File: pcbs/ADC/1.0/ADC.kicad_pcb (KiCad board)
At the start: 2 copper layers, 85 x 55 mm, 44 parts, among them J1 Conn_01x04_Pin, J3 Conn_01x02_Male, J4 Conn_01x03_Pin, J5 Conn_01x03_Pin, J9 Conn_01x04_Pin, U1 ZLDO1117QG33TA, U2 PCM1863, Y1 24.576 MHz

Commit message: Updating PCBs
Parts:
- moved C18 3.06 mm to (126.1, 102.4)
- moved R9 3.06 mm to (122.2, 102.4)
- moved C16 0.14 mm to (120.6, 92.1)
- renumbered C20 to C1, C4 to C10, C18 to C11, C19 to C12, C10 to C13, C11 to C14, C12 to C15, C13 to C16, C14 to C18, C15 to C19, C1 to C2, C16 to C20, C2 to C3, C6 to C4, C7 to C6, C8 to C7, C3 to C8, J3 to J2, J4 to J3, J9 to J4, R3 to R1, R8 to R2, R9 to R3, R1 to R4, R7 to R5, R2 to R7, R5 to R8, R4 to R9
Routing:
- net 3V3: track 120.4 -> 115.4 mm, vias 4 -> 2
- net 3V3A: track 83.7 -> 79.9 mm, vias 4 -> 2
- net GND: track 31.8 -> 29.8 mm
- net Net-(U2-VINL1): track 15.3 -> 17.3 mm
- net SCL: track 25.6 -> 26.7 mm
- net I2S_LRCLK_OUT: track 6.46 -> 5.57 mm
- net 5V: track 49.2 -> 50.0 mm, vias 0 -> 2

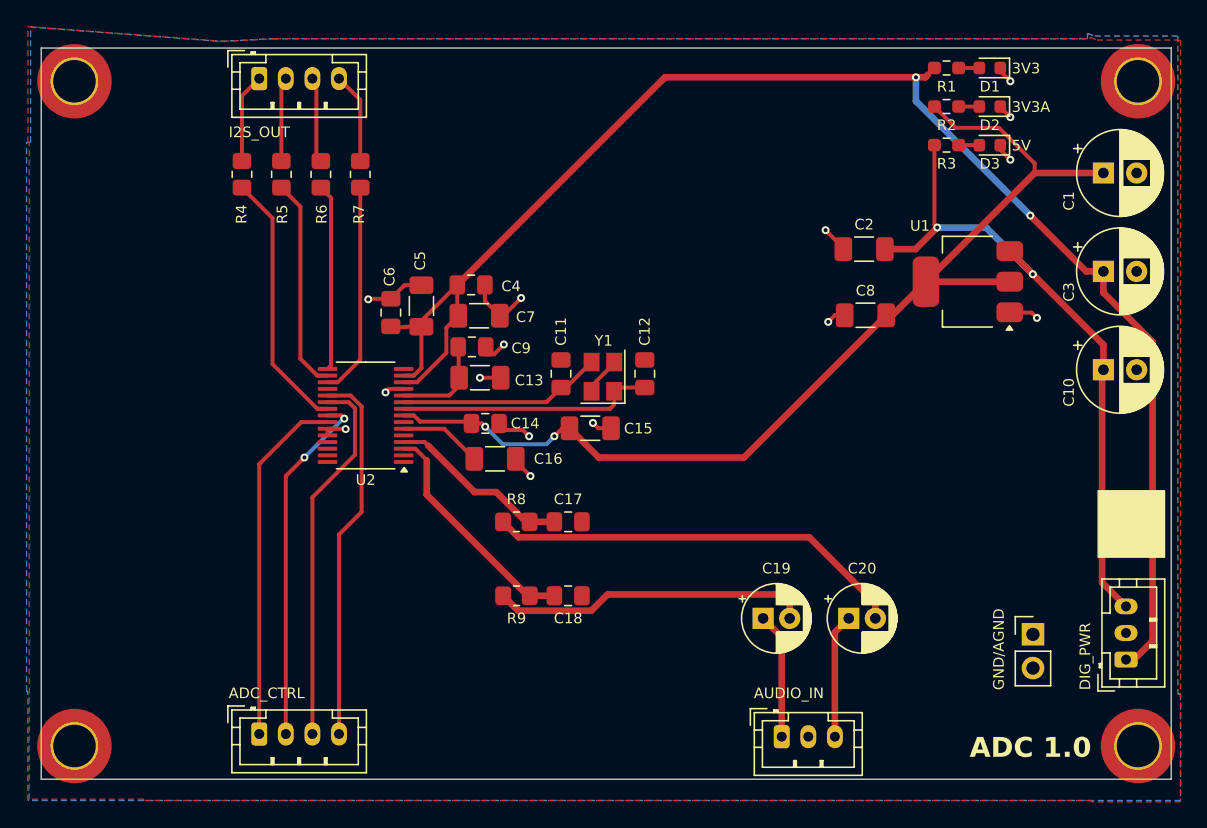
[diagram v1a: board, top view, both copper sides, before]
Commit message: Updated screenshots
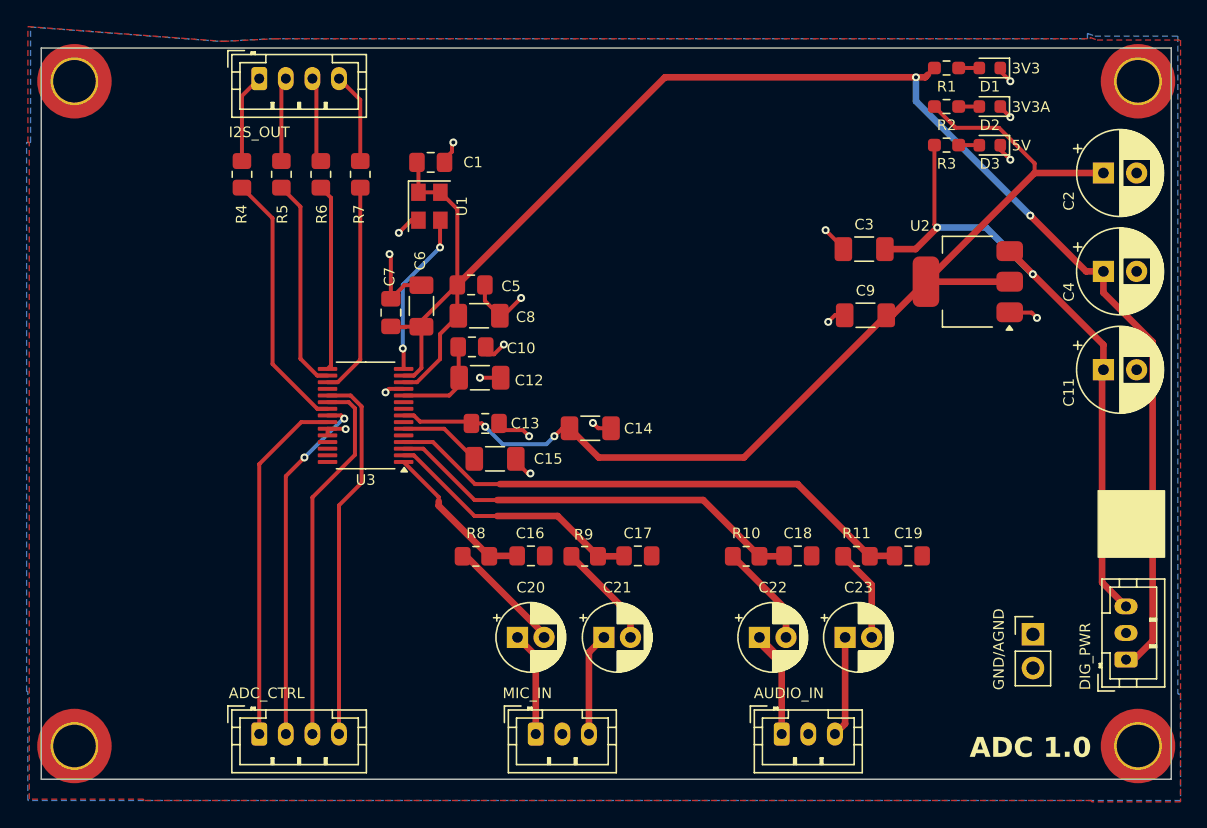
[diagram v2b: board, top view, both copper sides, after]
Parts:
- removed the C12 at (131.8, 85.7)
- removed Y1: 24.576 MHz, Crystal:Crystal_SMD_3225-4Pin_3.2x2.5mm
- added C16: 10n C0G, Capacitor_SMD:C_0805_2012Metric_Pad1.18x1.45mm_HandSolder, F.Cu at (123.3, 99.4)
- added C17: 10n C0G, Capacitor_SMD:C_0805_2012Metric_Pad1.18x1.45mm_HandSolder, F.Cu at (131.3, 99.4)
- added C20: 10u NICHICON 25V, Capacitor_THT:CP_Radial_D5.0mm_P2.00mm, F.Cu at (122.3, 105.5)
- added C21: 10u NICHICON 25V, Capacitor_THT:CP_Radial_D5.0mm_P2.00mm, F.Cu at (128.8, 105.5)
- added J5: Conn_01x03_Pin, Connector_JST:JST_PH_B3B-PH-K_1x03_P2.00mm_Vertical, F.Cu at (123.6, 112.8)
- added R8: 100R, Resistor_SMD:R_0805_2012Metric_Pad1.20x1.40mm_HandSolder, F.Cu at (119.1, 99.4)
- added R9: 100R, Resistor_SMD:R_0805_2012Metric_Pad1.20x1.40mm_HandSolder, F.Cu at (127.3, 99.4)
- added U1: ASDMB-xxxMHz, Oscillator:Oscillator_SMD_Abracon_ASE-4Pin_3.2x2.5mm, F.Cu at (115.6, 73.1)
- C1: renamed from C11; value 12n C0G -> 0.1u
- moved R11 25.7 mm to (147.8, 99.4)
- moved C19 25.7 mm to (151.7, 99.4)
- moved C1 18.7 mm to (115.7, 69.8), turned to 0 degrees
- moved C18 17.5 mm to (143.3, 99.4)
- moved R10 17.5 mm to (139.5, 99.4)
- moved C22 1.46 mm to (140.5, 105.5)
- moved C23 1.46 mm to (146.9, 105.5)
- moved J6 0.20 mm to (142.1, 112.8)
- renumbered C9 to C10, C10 to C11, C13 to C12, C14 to C13, C15 to C14, C16 to C15, C17 to C19, C1 to C2, C19 to C22, C20 to C23, C2 to C3, C3 to C4, C4 to C5, C5 to C6, C6 to C7, C7 to C8, C8 to C9, J5 to J6, R9 to R10, R8 to R11, U1 to U2, U2 to U3
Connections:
- C1 pad 1: XI -> 3V3
- C1 pad 2: AGND -> GND
- U3 pad 1: AGND -> Net-(U3-VINL2)
- U3 pad 10: XI -> unconnected-(U3-XI-Pad10)
- U3 pad 15: unconnected-(U2-SCLKI-Pad15) -> SCLKI
- U3 pad 2: AGND -> Net-(U3-VINR2)
- U3 pad 9: XO -> unconnected-(U3-XO-Pad9)
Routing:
- net Net-(U3-VINR1): track 13.5 -> 40.5 mm
- net Net-(C23-Pad2): track 31.7 -> 6.99 mm
- net Net-(U3-VINR2): track 0.00 -> 19.7 mm
- net XO: track 19.0 -> 0.00 mm
- net Net-(C22-Pad2): track 23.9 -> 7.76 mm
- net XI: track 15.0 -> 0.00 mm
- net Net-(U3-VINL1): track 17.3 -> 31.9 mm
- net SCLKI: track 0.00 -> 12.3 mm, vias 0 -> 2
- net Net-(U3-VINL2): track 0.00 -> 12.3 mm
- net 3V3: track 115.4 -> 126.0 mm
- net Net-(C20-Pad2): track 0.00 -> 8.80 mm
- net Net-(C21-Pad2): track 0.00 -> 7.94 mm
- net MIC_LEFT_IN: track 0.00 -> 7.84 mm
- net MIC_RIGHT_IN: track 0.00 -> 7.74 mm
- net GND: track 29.8 -> 34.7 mm, vias 15 -> 17
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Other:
- board text added: "MIC_IN"
